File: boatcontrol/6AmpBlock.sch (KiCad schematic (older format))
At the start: 15 parts, among them U7901 ULN2803A

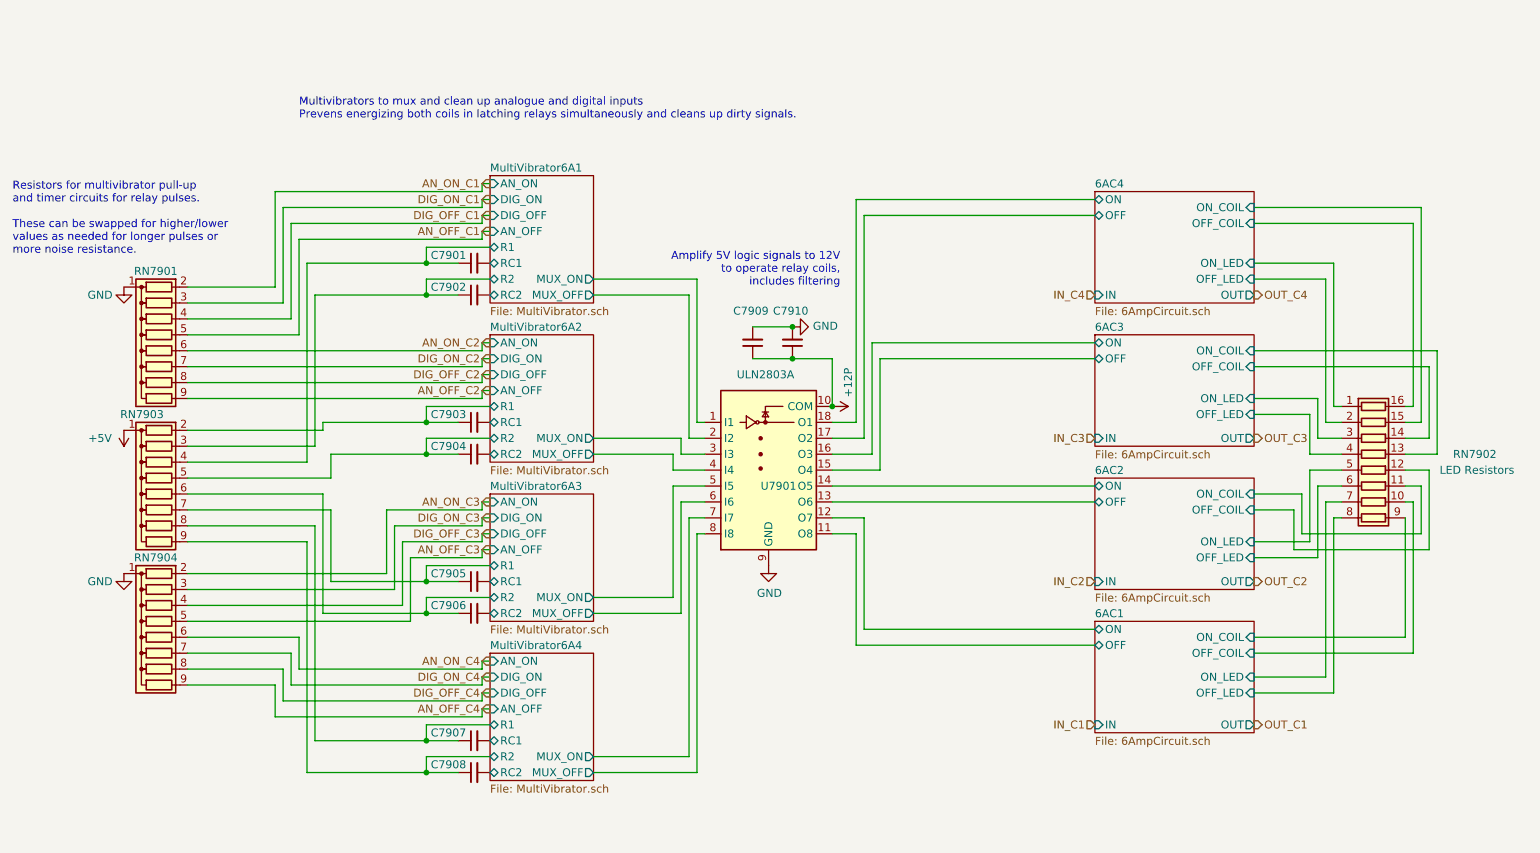
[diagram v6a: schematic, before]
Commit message: Add xors on input
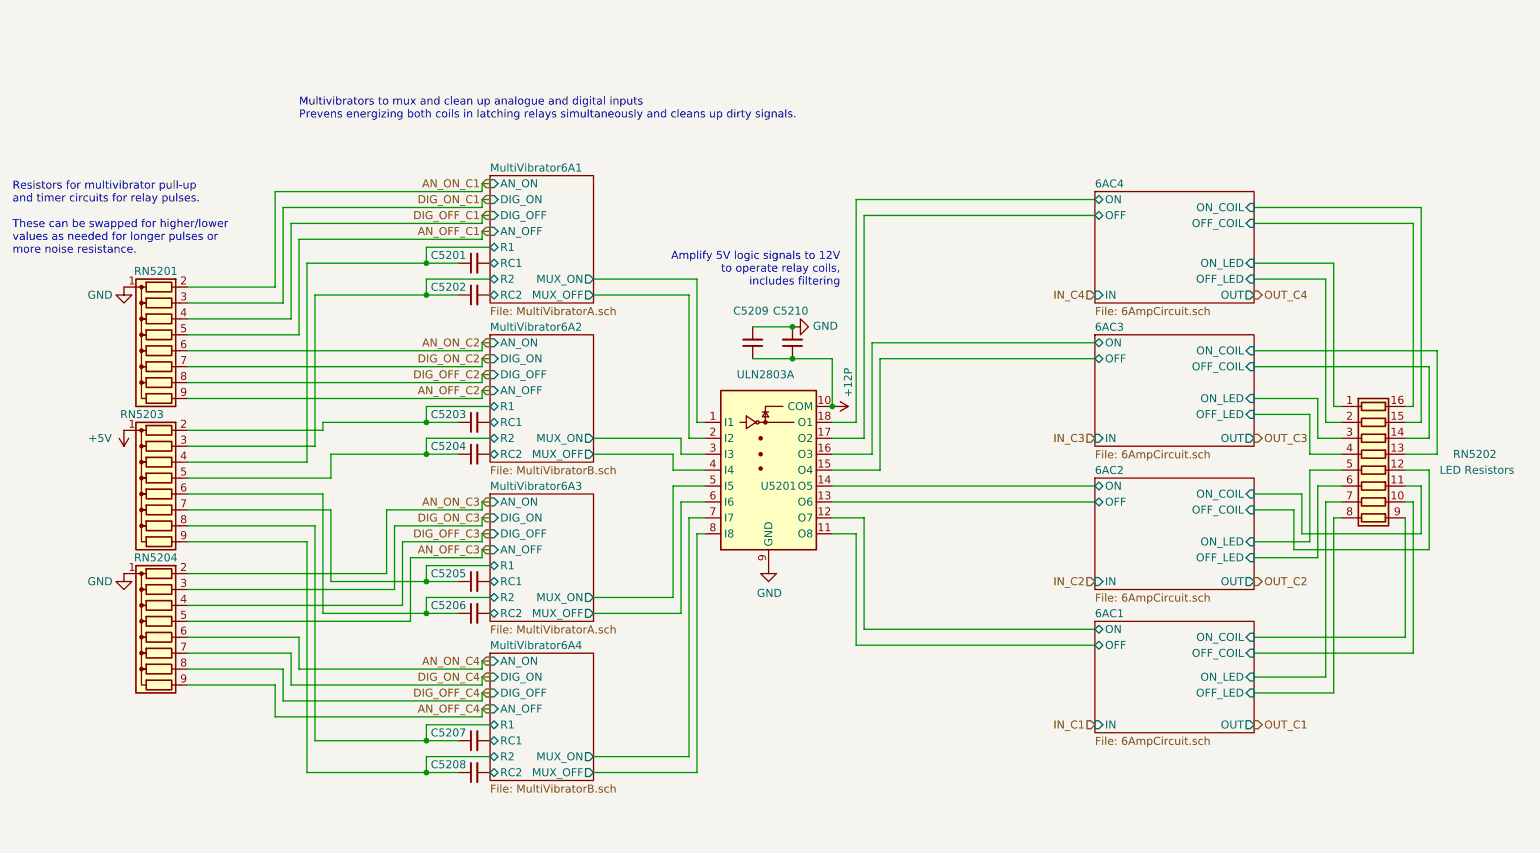
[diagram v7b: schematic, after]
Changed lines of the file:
@@
 $Descr A4 11693 8268
 encoding utf-8
-Sheet 67 97
+Sheet 40 97
 Title "Boat Control Hat"
 Date "2020-07-09"
@@
 AR Path="/D1BB8DB4/5F317CB5/60365AE4" Ref="#PWR07901"  Part="1"
 AR Path="/D1BB8DB4/5F746103/60365AE4" Ref="#PWR05201"  Part="1"
-F 0 "#PWR07901" H 6700 3400 50  0001 C CNN
+F 0 "#PWR05201" H 6700 3400 50  0001 C CNN
 F 1 "+12P" H 6550 3650 50  0000 C CNN
 F 2 "" H 6700 3550 50  0001 C CNN
@@
 AR Path="/D1BB8DB4/5F317CB5/60365AF1" Ref="U7901"  Part="1"
 AR Path="/D1BB8DB4/5F746103/60365AF1" Ref="U5201"  Part="1"
-F 0 "U7901" H 6250 3650 50  0000 L CNN
+F 0 "U5201" H 6250 3650 50  0000 L CNN
 F 1 "ULN2803A" H 6100 4350 50  0000 L CNN
 F 2 "Package_DIP:DIP-18_W7.62mm" H 6350 3200 50  0001 L CNN
@@
 AR Path="/D1BB8DB4/5F317CB5/60365B03" Ref="#PWR07902"  Part="1"
 AR Path="/D1BB8DB4/5F746103/60365B03" Ref="#PWR05202"  Part="1"
-F 0 "#PWR07902" H 6300 4300 50  0001 C CNN
+F 0 "#PWR05202" H 6300 4300 50  0001 C CNN
 F 1 "GND" H 6305 4377 50  0000 C CNN
 F 2 "" H 6300 4550 50  0001 C CNN
@@
 U 60365B0F
 F0 "MultiVibrator6A1" 50
-F1 "MultiVibrator.sch" 50
+F1 "MultiVibratorA.sch" 50
 F2 "DIG_OFF" I L 4550 2350 50
 F3 "AN_OFF" I L 4550 2450 50
@@
 U 60365B29
 F0 "MultiVibrator6A2" 50
-F1 "MultiVibrator.sch" 50
+F1 "MultiVibratorB.sch" 50
 F2 "DIG_OFF" I L 4550 3350 50
 F3 "AN_OFF" I L 4550 3450 50
@@
 U 60365B35
 F0 "MultiVibrator6A3" 50
-F1 "MultiVibrator.sch" 50
+F1 "MultiVibratorA.sch" 50
 F2 "DIG_OFF" I L 4550 4350 50
 F3 "AN_OFF" I L 4550 4450 50
@@
 U 60365B41
 F0 "MultiVibrator6A4" 50
-F1 "MultiVibrator.sch" 50
+F1 "MultiVibratorB.sch" 50
 F2 "DIG_OFF" I L 4550 5350 50
 F3 "AN_OFF" I L 4550 5450 50
@@
 AR Path="/D1BB8DB4/5F317CB5/60365C68" Ref="RN7902"  Part="1"
 AR Path="/D1BB8DB4/5F746103/60365C68" Ref="RN5202"  Part="1"
-F 0 "RN7902" V 10000 4450 50  0000 L CNN
+F 0 "RN5202" V 10000 4450 50  0000 L CNN
 F 1 "680Ω" V 9600 3800 50  0001 L CNN
 F 2 "BoatControl:DIP254P762X432-16P" V 10575 3950 50  0001 C CNN
@@
 AR Path="/D1BB8DB4/5F746103/62AB509B" Ref="C5201"  Part="1"
 AR Path="/D1BB8DB4/5F317CB5/62AB509B" Ref="C7901"  Part="1"
-F 0 "C7901" V 4400 2700 50  0000 L CNN
+F 0 "C5201" V 4400 2700 50  0000 L CNN
 F 1 "1µF" H 3600 2550 50  0001 L CNN
 F 2 "Capacitor_THT:C_Disc_D7.5mm_W5.0mm_P5.00mm" H 4450 2650 50  0001 C CNN
@@
 AR Path="/D1BB8DB4/5F746103/62AC1E93" Ref="C5202"  Part="1"
 AR Path="/D1BB8DB4/5F317CB5/62AC1E93" Ref="C7902"  Part="1"
-F 0 "C7902" V 4400 2900 50  0000 L CNN
+F 0 "C5202" V 4400 2900 50  0000 L CNN
 F 1 "1µF" H 3600 2750 50  0001 L CNN
 F 2 "Capacitor_THT:C_Disc_D7.5mm_W5.0mm_P5.00mm" H 4450 2850 50  0001 C CNN
@@
 AR Path="/D1BB8DB4/5F746103/62ADD9A6" Ref="C5208"  Part="1"
 AR Path="/D1BB8DB4/5F317CB5/62ADD9A6" Ref="C7908"  Part="1"
-F 0 "C7908" V 4400 5900 50  0000 L CNN
+F 0 "C5208" V 4400 5900 50  0000 L CNN
 F 1 "1µF" H 3600 5750 50  0001 L CNN
 F 2 "Capacitor_THT:C_Disc_D7.5mm_W5.0mm_P5.00mm" H 4450 5850 50  0001 C CNN
@@
 AR Path="/D1BB8DB4/5F746103/62AEACF8" Ref="C5207"  Part="1"
 AR Path="/D1BB8DB4/5F317CB5/62AEACF8" Ref="C7907"  Part="1"
-F 0 "C7907" V 4400 5700 50  0000 L CNN
+F 0 "C5207" V 4400 5700 50  0000 L CNN
 F 1 "1µF" H 3600 5550 50  0001 L CNN
 F 2 "Capacitor_THT:C_Disc_D7.5mm_W5.0mm_P5.00mm" H 4450 5650 50  0001 C CNN
@@
 AR Path="/D1BB8DB4/5F746103/62AF81A3" Ref="C5206"  Part="1"
 AR Path="/D1BB8DB4/5F317CB5/62AF81A3" Ref="C7906"  Part="1"
-F 0 "C7906" V 4400 4900 50  0000 L CNN
+F 0 "C5206" V 4400 4900 50  0000 L CNN
 F 1 "1µF" H 3600 4750 50  0001 L CNN
 F 2 "Capacitor_THT:C_Disc_D7.5mm_W5.0mm_P5.00mm" H 4450 4850 50  0001 C CNN
@@
 AR Path="/D1BB8DB4/5F746103/62B05762" Ref="C5205"  Part="1"
 AR Path="/D1BB8DB4/5F317CB5/62B05762" Ref="C7905"  Part="1"
-F 0 "C7905" V 4400 4700 50  0000 L CNN
+F 0 "C5205" V 4400 4700 50  0000 L CNN
 F 1 "1µF" H 3600 4550 50  0001 L CNN
 F 2 "Capacitor_THT:C_Disc_D7.5mm_W5.0mm_P5.00mm" H 4450 4650 50  0001 C CNN
@@
 AR Path="/D1BB8DB4/5F746103/62B3C5BA" Ref="C5203"  Part="1"
 AR Path="/D1BB8DB4/5F317CB5/62B3C5BA" Ref="C7903"  Part="1"
-F 0 "C7903" V 4400 3700 50  0000 L CNN
+F 0 "C5203" V 4400 3700 50  0000 L CNN
 F 1 "1µF" H 3600 3550 50  0001 L CNN
 F 2 "Capacitor_THT:C_Disc_D7.5mm_W5.0mm_P5.00mm" H 4450 3650 50  0001 C CNN
@@
 AR Path="/D1BB8DB4/5F746103/62B4996D" Ref="C5204"  Part="1"
 AR Path="/D1BB8DB4/5F317CB5/62B4996D" Ref="C7904"  Part="1"
-F 0 "C7904" V 4400 3900 50  0000 L CNN
+F 0 "C5204" V 4400 3900 50  0000 L CNN
 F 1 "1µF" H 3600 3750 50  0001 L CNN
 F 2 "Capacitor_THT:C_Disc_D7.5mm_W5.0mm_P5.00mm" H 4450 3850 50  0001 C CNN
@@
 AR Path="/D1BB8DB4/5F317CB5/62C7A7CE" Ref="RN7903"  Part="1"
 AR Path="/D1BB8DB4/5F746103/62C7A7CE" Ref="RN5203"  Part="1"
-F 0 "RN7903" V 1950 4050 50  0000 L CNN
+F 0 "RN5203" V 1950 4050 50  0000 L CNN
 F 1 "10MΩ" H 2100 3700 50  0001 L CNN
 F 2 "Resistor_THT:R_Array_SIP9" V 2925 4100 50  0001 C CNN
@@
 AR Path="/D1BB8DB4/5F317CB5/62F1D24C" Ref="RN7904"  Part="1"
 AR Path="/D1BB8DB4/5F746103/62F1D24C" Ref="RN5204"  Part="1"
-F 0 "RN7904" V 1950 5000 50  0000 C CNN
+F 0 "RN5204" V 1950 5000 50  0000 C CNN
 F 1 "100KΩ" V 2250 4700 50  0001 C CNN
 F 2 "Resistor_THT:R_Array_SIP9" H 3200 5100 50  0001 L CNN
@@
 AR Path="/D1BB8DB4/5F317CB5/62F2A731" Ref="RN7901"  Part="1"
 AR Path="/D1BB8DB4/5F746103/62F2A731" Ref="RN5201"  Part="1"
-F 0 "RN7901" V 1950 3200 50  0000 C CNN
+F 0 "RN5201" V 1950 3200 50  0000 C CNN
 F 1 "100KΩ" V 2250 2900 50  0001 C CNN
 F 2 "Resistor_THT:R_Array_SIP9" H 3200 3300 50  0001 L CNN
@@
 AR Path="/D1BB8DB4/5F317CB5/624D8B2F" Ref="C7909"  Part="1"
 AR Path="/D1BB8DB4/5F746103/624D8B2F" Ref="C5209"  Part="1"
-F 0 "C7909" H 6100 2950 50  0000 L CNN
+F 0 "C5209" H 6100 2950 50  0000 L CNN
 F 1 "10uF" H 6291 3105 50  0001 L CNN
 F 2 "Capacitor_THT:C_Disc_D7.5mm_W5.0mm_P5.00mm" H 6200 3150 50  0001 C CNN
@@
 AR Path="/D1BB8DB4/5F317CB5/624D8B37" Ref="C7910"  Part="1"
 AR Path="/D1BB8DB4/5F746103/624D8B37" Ref="C5210"  Part="1"
-F 0 "C7910" H 6350 2950 50  0000 L CNN
+F 0 "C5210" H 6350 2950 50  0000 L CNN
 F 1 "0.1uF" H 6541 3105 50  0001 L CNN
 F 2 "Capacitor_THT:C_Disc_D7.5mm_W5.0mm_P5.00mm" H 6450 3150 50  0001 C CNN
@@
 AR Path="/D1BB8DB4/5F317CB5/624D8B3E" Ref="#PWR0204"  Part="1"
 AR Path="/D1BB8DB4/5F746103/624D8B3E" Ref="#PWR0198"  Part="1"
-F 0 "#PWR0204" H 6450 2800 50  0001 C CNN
+F 0 "#PWR0198" H 6450 2800 50  0001 C CNN
 F 1 "GND" V 6455 2922 50  0000 R CNN
 F 2 "" H 6450 3050 50  0001 C CNN
@@
 AR Path="/D16552B4/5FA17F6C/6027D066" Ref="#PWR?"  Part="1"
 AR Path="/D16552B4/5FA17F86/6027D066" Ref="#PWR?"  Part="1"
+AR Path="/D1BB8DB4/5F317CB5/6027D066" Ref="#PWR?"  Part="1"
+AR Path="/D1BB8DB4/5F746103/6027D066" Ref="#PWR?"  Part="1"
 F 0 "#PWR?" H 2250 3550 50  0001 C CNN
 F 1 "+5V" H 2400 3750 50  0000 C CNN
@@
 U 1 1 6027D06C
 P 2250 2800
+AR Path="/D1BB8DB4/5F317CB5/6027D06C" Ref="#PWR?"  Part="1"
+AR Path="/D1BB8DB4/5F746103/6027D06C" Ref="#PWR?"  Part="1"
 F 0 "#PWR?" H 2250 2550 50  0001 C CNN
 F 1 "GND" H 2100 2750 50  0000 C CNN
@@
 U 1 1 6027D072
 P 2250 4600
+AR Path="/D1BB8DB4/5F317CB5/6027D072" Ref="#PWR?"  Part="1"
+AR Path="/D1BB8DB4/5F746103/6027D072" Ref="#PWR?"  Part="1"
 F 0 "#PWR?" H 2250 4350 50  0001 C CNN
 F 1 "GND" H 2100 4550 50  0000 C CNN
